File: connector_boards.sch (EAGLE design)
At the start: 3 parts

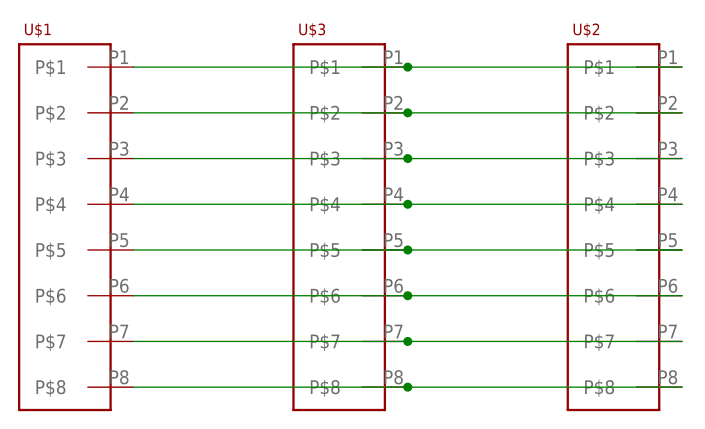
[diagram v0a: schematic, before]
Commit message: Return to the original state after major disruption
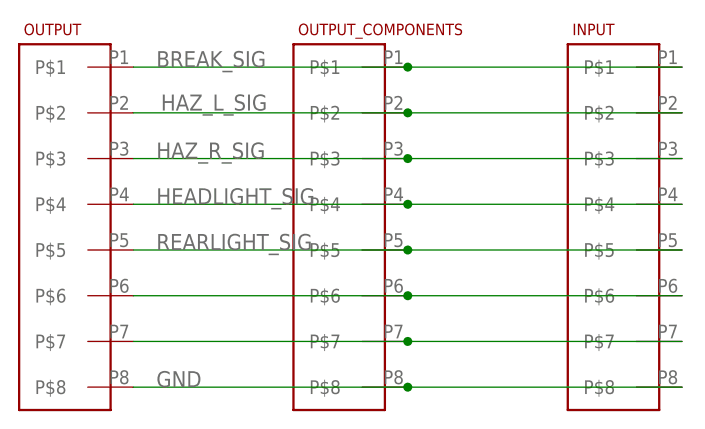
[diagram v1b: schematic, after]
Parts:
- renumbered U$1 to OUTPUT, U$2 to INPUT, U$3 to OUTPUT_COMPONENTS
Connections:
- net N$1 renamed BREAK_SIG
- net N$2 renamed HAZ_L_SIG
- net N$3 renamed HAZ_R_SIG
- net N$4 renamed HEADLIGHT_SIG
- net N$5 renamed REARLIGHT_SIG
- net N$8 renamed GND
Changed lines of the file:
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@@
 <layer number="91" name="Nets" color="2" fill="1" visible="yes" active="yes"/>
 <layer number="92" name="Busses" color="1" fill="1" visible="yes" active="yes"/>
-<layer number="93" name="Pins" color="2" fill="1" visible="no" active="yes"/>
+<layer number="93" name="Pins" color="2" fill="1" visible="yes" active="yes"/>
 <layer number="94" name="Symbols" color="4" fill="1" visible="yes" active="yes"/>
 <layer number="95" name="Names" color="7" fill="1" visible="yes" active="yes"/>
@@
 </classes>
 <parts>
-<part name="U$1" library="master_library" deviceset="8-PIN-MOLEX-RA-FEMALE" device=""/>
-<part name="U$2" library="master_library" deviceset="8-PIN-MOLEX-RA-FEMALE" device=""/>
-<part name="U$3" library="master_library" deviceset="8-PIN-MOLEX-RA-FEMALE" device=""/>
+<part name="OUTPUT" library="master_library" deviceset="8-PIN-MOLEX-RA-FEMALE" device=""/>
+<part name="INPUT" library="master_library" deviceset="8-PIN-MOLEX-RA-FEMALE" device=""/>
+<part name="OUTPUT_COMPONENTS" library="master_library" deviceset="8-PIN-MOLEX-RA-FEMALE" device=""/>
 </parts>
 <sheets>
@@
 </plain>
 <instances>
-<instance part="U$1" gate="G$1" x="27.94" y="73.66"/>
-<instance part="U$2" gate="G$1" x="88.9" y="73.66"/>
-<instance part="U$3" gate="G$1" x="58.42" y="73.66"/>
+<instance part="OUTPUT" gate="G$1" x="27.94" y="73.66"/>
+<instance part="INPUT" gate="G$1" x="88.9" y="73.66"/>
+<instance part="OUTPUT_COMPONENTS" gate="G$1" x="58.42" y="73.66"/>
 </instances>
 <busses>
 </busses>
 <nets>
-<net name="N$1" class="0">
+<net name="BREAK_SIG" class="0">
 <segment>
-<pinref part="U$1" gate="G$1" pin="P$1"/>
-<pinref part="U$2" gate="G$1" pin="P$1"/>
+<pinref part="OUTPUT" gate="G$1" pin="P$1"/>
+<pinref part="INPUT" gate="G$1" pin="P$1"/>
 <wire x1="35.56" y1="86.36" x2="66.04" y2="86.36" width="0.1524" layer="91"/>
-<pinref part="U$3" gate="G$1" pin="P$1"/>
+<pinref part="OUTPUT_COMPONENTS" gate="G$1" pin="P$1"/>
 <wire x1="66.04" y1="86.36" x2="96.52" y2="86.36" width="0.1524" layer="91"/>
 <junction x="66.04" y="86.36"/>
+<label x="38.1" y="86.36" size="1.778" layer="95"/>
 </segment>
 </net>
-<net name="N$2" class="0">
+<net name="HAZ_L_SIG" class="0">
 <segment>
-<pinref part="U$1" gate="G$1" pin="P$2"/>
-<pinref part="U$2" gate="G$1" pin="P$2"/>
+<pinref part="OUTPUT" gate="G$1" pin="P$2"/>
+<pinref part="INPUT" gate="G$1" pin="P$2"/>
 <wire x1="35.56" y1="81.28" x2="66.04" y2="81.28" width="0.1524" layer="91"/>
-<pinref part="U$3" gate="G$1" pin="P$2"/>
+<pinref part="OUTPUT_COMPONENTS" gate="G$1" pin="P$2"/>
 <wire x1="66.04" y1="81.28" x2="96.52" y2="81.28" width="0.1524" layer="91"/>
 <junction x="66.04" y="81.28"/>
+<label x="38.608" y="81.534" size="1.778" layer="95"/>
 </segment>
 </net>
-<net name="N$3" class="0">
+<net name="HAZ_R_SIG" class="0">
 <segment>
-<pinref part="U$1" gate="G$1" pin="P$3"/>
-<pinref part="U$2" gate="G$1" pin="P$3"/>
+<pinref part="OUTPUT" gate="G$1" pin="P$3"/>
+<pinref part="INPUT" gate="G$1" pin="P$3"/>
 <wire x1="35.56" y1="76.2" x2="66.04" y2="76.2" width="0.1524" layer="91"/>
-<pinref part="U$3" gate="G$1" pin="P$3"/>
+<pinref part="OUTPUT_COMPONENTS" gate="G$1" pin="P$3"/>
 <wire x1="66.04" y1="76.2" x2="96.52" y2="76.2" width="0.1524" layer="91"/>
 <junction x="66.04" y="76.2"/>
+<label x="38.1" y="76.2" size="1.778" layer="95"/>
 </segment>
 </net>
-<net name="N$4" class="0">
+<net name="HEADLIGHT_SIG" class="0">
 <segment>
-<pinref part="U$1" gate="G$1" pin="P$4"/>
-<pinref part="U$2" gate="G$1" pin="P$4"/>
+<pinref part="OUTPUT" gate="G$1" pin="P$4"/>
+<pinref part="INPUT" gate="G$1" pin="P$4"/>
 <wire x1="35.56" y1="71.12" x2="66.04" y2="71.12" width="0.1524" layer="91"/>
-<pinref part="U$3" gate="G$1" pin="P$4"/>
+<pinref part="OUTPUT_COMPONENTS" gate="G$1" pin="P$4"/>
 <wire x1="66.04" y1="71.12" x2="96.52" y2="71.12" width="0.1524" layer="91"/>
 <junction x="66.04" y="71.12"/>
+<label x="38.1" y="71.12" size="1.778" layer="95"/>
 </segment>
 </net>
-<net name="N$5" class="0">
+<net name="REARLIGHT_SIG" class="0">
 <segment>
-<pinref part="U$1" gate="G$1" pin="P$5"/>
-<pinref part="U$2" gate="G$1" pin="P$5"/>
+<pinref part="OUTPUT" gate="G$1" pin="P$5"/>
+<pinref part="INPUT" gate="G$1" pin="P$5"/>
 <wire x1="35.56" y1="66.04" x2="66.04" y2="66.04" width="0.1524" layer="91"/>
-<pinref part="U$3" gate="G$1" pin="P$5"/>
+<pinref part="OUTPUT_COMPONENTS" gate="G$1" pin="P$5"/>
 <wire x1="66.04" y1="66.04" x2="96.52" y2="66.04" width="0.1524" layer="91"/>
 <junction x="66.04" y="66.04"/>
+<label x="38.1" y="66.04" size="1.778" layer="95"/>
 </segment>
 </net>
 <net name="N$6" class="0">
 <segment>
-<pinref part="U$1" gate="G$1" pin="P$6"/>
-<pinref part="U$2" gate="G$1" pin="P$6"/>
+<pinref part="OUTPUT" gate="G$1" pin="P$6"/>
+<pinref part="INPUT" gate="G$1" pin="P$6"/>
 <wire x1="35.56" y1="60.96" x2="66.04" y2="60.96" width="0.1524" layer="91"/>
-<pinref part="U$3" gate="G$1" pin="P$6"/>
+<pinref part="OUTPUT_COMPONENTS" gate="G$1" pin="P$6"/>
 <wire x1="66.04" y1="60.96" x2="96.52" y2="60.96" width="0.1524" layer="91"/>
 <junction x="66.04" y="60.96"/>
@@
 <net name="N$7" class="0">
 <segment>
-<pinref part="U$1" gate="G$1" pin="P$7"/>
-<pinref part="U$2" gate="G$1" pin="P$7"/>
+<pinref part="OUTPUT" gate="G$1" pin="P$7"/>
+<pinref part="INPUT" gate="G$1" pin="P$7"/>
 <wire x1="35.56" y1="55.88" x2="66.04" y2="55.88" width="0.1524" layer="91"/>
-<pinref part="U$3" gate="G$1" pin="P$7"/>
+<pinref part="OUTPUT_COMPONENTS" gate="G$1" pin="P$7"/>
 <wire x1="66.04" y1="55.88" x2="96.52" y2="55.88" width="0.1524" layer="91"/>
 <junction x="66.04" y="55.88"/>
 </segment>
 </net>
-<net name="N$8" class="0">
+<net name="GND" class="0">
 <segment>
-<pinref part="U$1" gate="G$1" pin="P$8"/>
-<pinref part="U$2" gate="G$1" pin="P$8"/>
+<pinref part="OUTPUT" gate="G$1" pin="P$8"/>
+<pinref part="INPUT" gate="G$1" pin="P$8"/>
 <wire x1="35.56" y1="50.8" x2="66.04" y2="50.8" width="0.1524" layer="91"/>
-<pinref part="U$3" gate="G$1" pin="P$8"/>
+<pinref part="OUTPUT_COMPONENTS" gate="G$1" pin="P$8"/>
 <wire x1="66.04" y1="50.8" x2="96.52" y2="50.8" width="0.1524" layer="91"/>
 <junction x="66.04" y="50.8"/>
+<label x="38.1" y="50.8" size="1.778" layer="95"/>
 </segment>
 </net>
